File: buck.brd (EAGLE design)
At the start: 100 x 100 mm, 30 parts, among them J1 B06B-HCMKK, J2 POWERPOLE_POWER45A_DRILL, J3 POWERPOLE_POWER45A_DRILL

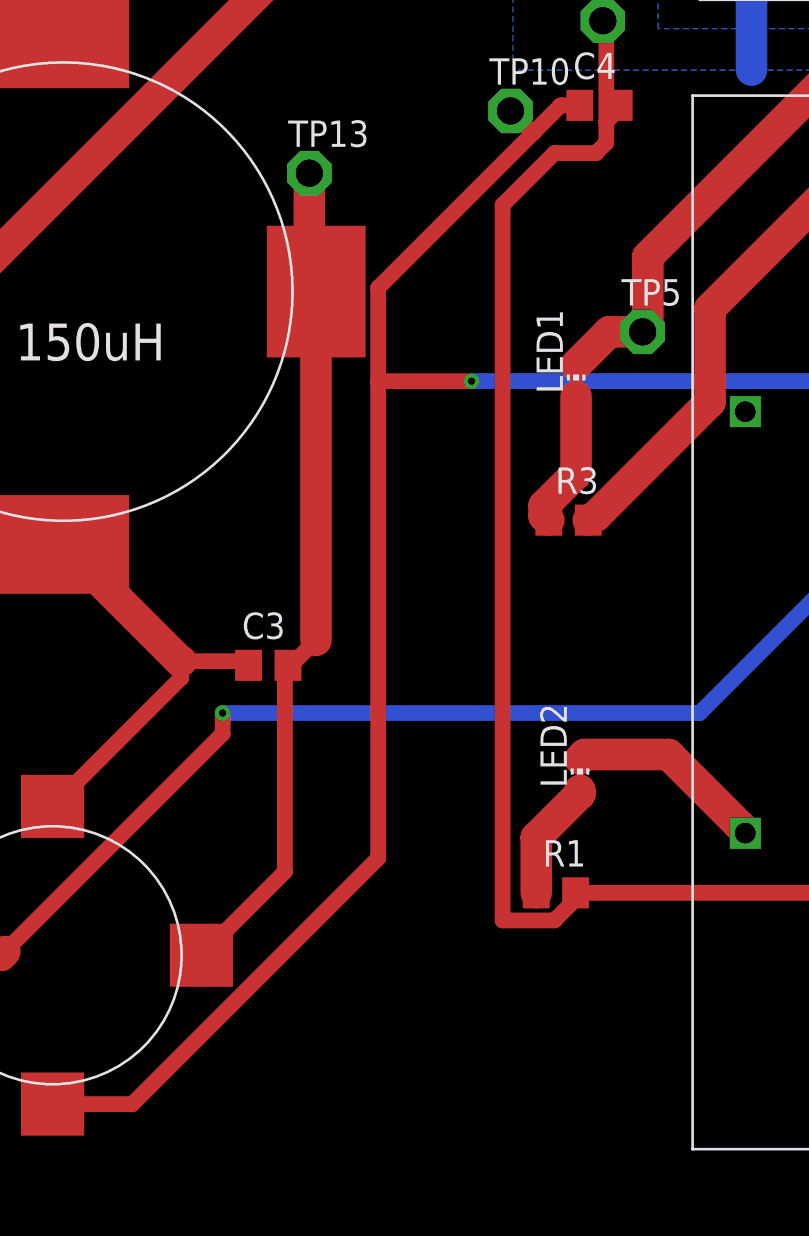
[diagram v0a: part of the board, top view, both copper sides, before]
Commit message: fixed pad clearance
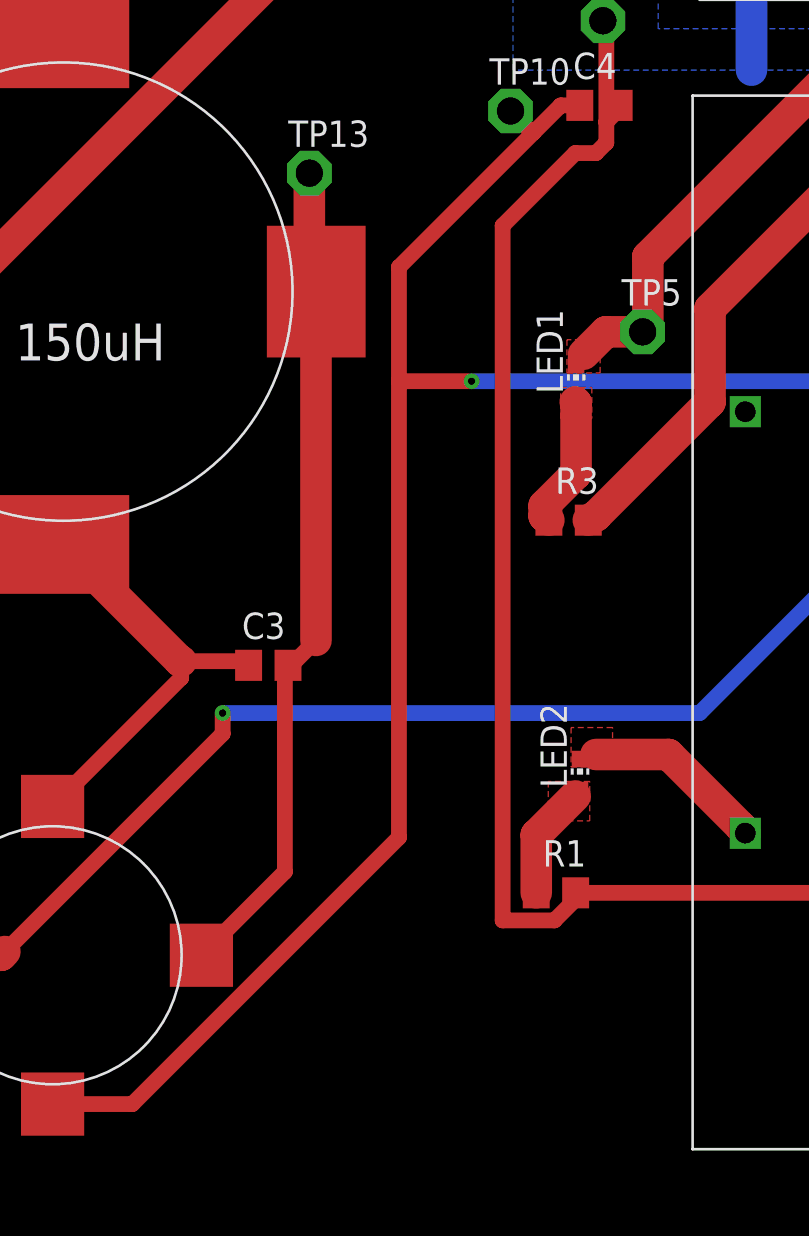
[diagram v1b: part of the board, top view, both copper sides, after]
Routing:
- net N$8: track 122.4 -> 121.4 mm
- net GND: track 109.4 -> 108.6 mm
- net 1.6A_OUT: track 161.3 -> 160.7 mm
- net 6A_GND: track 22.6 -> 22.0 mm
- added copper zone on layer 1, net 6A_GND
- added copper zone on layer 1, net GND
- added copper zone on layer 1, net N$10
- added copper zone on layer 1, net N$24
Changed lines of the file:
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@@
 <?xml version="1.0" encoding="utf-8"?>
 <!DOCTYPE eagle SYSTEM "eagle.dtd">
-<eagle version="9.5.1">
+<eagle version="9.5.0">
 <drawing>
 <settings>
@@
 <wire x1="51.5" y1="36.5" x2="51.5" y2="37" width="1.524" layer="1"/>
 <wire x1="51.5" y1="36.5" x2="51.73" y2="36.3" width="1.524" layer="1"/>
-<wire x1="53.04" y1="38.54" x2="51.5" y2="37" width="1.524" layer="1"/>
-<wire x1="53.04" y1="42.28" x2="53.04" y2="38.54" width="1.524" layer="1"/>
+<wire x1="51.5" y1="37" x2="53.04" y2="38.54" width="1.524" layer="1"/>
+<polygon width="0" layer="1" thermals="no">
+<vertex x="52.3" y="42.7"/>
+<vertex x="53.8" y="42.7"/>
+<vertex x="53.8" y="41.2"/>
+<vertex x="52.3" y="41.2"/>
+</polygon>
+<wire x1="53.04" y1="38.54" x2="53.04" y2="41.96" width="1.524" layer="1"/>
+<wire x1="53.04" y1="41.96" x2="53" y2="42" width="1.524" layer="1"/>
 </signal>
 <signal name="GND" class="1">
@@
 <contactref element="U$3" pad="-VOUT"/>
 <contactref element="C5" pad="2"/>
-<polygon width="0.1524" layer="16">
+<polygon width="0.1524" layer="16" thermals="no">
 <vertex x="50" y="82"/>
 <vertex x="35" y="82"/>
@@
 <via x="32" y="96" extent="1-16" drill="0.35"/>
 <via x="85.5" y="58" extent="1-16" drill="0.35"/>
-<wire x1="53.23" y1="24.78" x2="53.45" y2="25" width="1.524" layer="1"/>
-<wire x1="53.45" y1="25" x2="57.5" y2="25" width="1.524" layer="1"/>
 <wire x1="10.49" y1="58.38" x2="27.188" y2="58.38" width="1.524" layer="1"/>
 <wire x1="27.188" y1="58.38" x2="28.32" y2="59.512" width="1.524" layer="1"/>
+<polygon width="0" layer="1" thermals="no">
+<vertex x="52.8" y="26.3"/>
+<vertex x="52.8" y="24.4"/>
+<vertex x="54.8" y="24.4"/>
+<vertex x="54.8" y="26.3"/>
+</polygon>
+<wire x1="57.5" y1="25" x2="54" y2="25" width="1.524" layer="1"/>
 </signal>
 <signal name="BAT_OUT" class="1">
@@
 <wire x1="54" y1="54" x2="54.5" y2="54.5" width="0.762" layer="1"/>
 <wire x1="54.5" y1="55.5" x2="55" y2="56" width="0.762" layer="1"/>
-<wire x1="52" y1="54" x2="54" y2="54" width="0.762" layer="1"/>
-<wire x1="49.5" y1="51.5" x2="52" y2="54" width="0.762" layer="1"/>
-<wire x1="49.5" y1="17" x2="49.5" y2="51.5" width="0.762" layer="1"/>
+<wire x1="53" y1="54" x2="54" y2="54" width="0.762" layer="1"/>
+<wire x1="49.5" y1="50.5" x2="53" y2="54" width="0.762" layer="1"/>
+<wire x1="49.5" y1="17" x2="49.5" y2="50.5" width="0.762" layer="1"/>
 <wire x1="49.5" y1="17" x2="52" y2="17" width="0.762" layer="1"/>
 <wire x1="55" y1="56" x2="55.12" y2="56.3" width="0.762" layer="1"/>
@@
 <contactref element="U$1" pad="-S"/>
 <contactref element="LED1" pad="C"/>
-<polygon width="0.1524" layer="16">
+<polygon width="0.1524" layer="16" thermals="no">
 <vertex x="104" y="101"/>
 <vertex x="104" y="62"/>
@@
 <via x="66" y="58.5" extent="1-16" drill="0.35"/>
 <wire x1="56.25" y1="45.38" x2="56.5" y2="45.5" width="1.524" layer="1"/>
-<wire x1="56.25" y1="45.38" x2="54.64" y2="45.38" width="1.524" layer="1"/>
-<wire x1="54.64" y1="45.38" x2="53.04" y2="43.78" width="1.524" layer="1"/>
 <wire x1="56.5" y1="49" x2="66" y2="58.5" width="1.524" layer="1"/>
 <wire x1="56.5" y1="45.5" x2="56.5" y2="49" width="1.524" layer="1"/>
+<polygon width="0" layer="1" thermals="no">
+<vertex x="52.6" y="45"/>
+<vertex x="52.6" y="43.4"/>
+<vertex x="54.2" y="43.4"/>
+<vertex x="54.2" y="45"/>
+</polygon>
+<wire x1="54.48" y1="45.38" x2="53.4" y2="44.3" width="1.524" layer="1"/>
+<wire x1="56.25" y1="45.38" x2="54.48" y2="45.38" width="1.524" layer="1"/>
+<wire x1="53.4" y1="44.3" x2="53.04" y2="43.78" width="0" layer="19" extent="1-1"/>
 </signal>
 <signal name="6A_OUT" class="1">
@@
 <wire x1="69" y1="42" x2="83.5" y2="56.5" width="0.762" layer="1"/>
 <wire x1="69" y1="42" x2="68.82" y2="41.53" width="0.762" layer="1"/>
-<wire x1="43.5" y1="47.5" x2="51" y2="55" width="0.762" layer="1"/>
+<wire x1="44.5" y1="48.5" x2="51" y2="55" width="0.762" layer="1"/>
 <wire x1="51" y1="55" x2="52.3" y2="56.3" width="0.762" layer="1"/>
 <wire x1="53.22" y1="56.3" x2="52.3" y2="56.3" width="0.762" layer="1"/>
-<wire x1="43.5" y1="43" x2="43.5" y2="20" width="0.762" layer="1"/>
-<wire x1="43.5" y1="43" x2="43.5" y2="47.5" width="0.762" layer="1"/>
+<wire x1="44.5" y1="43" x2="44.5" y2="21" width="0.762" layer="1"/>
+<wire x1="44.5" y1="43" x2="44.5" y2="48.5" width="0.762" layer="1"/>
 <wire x1="68.5" y1="43" x2="68.5" y2="42" width="0.762" layer="16"/>
 <wire x1="68.5" y1="43" x2="48" y2="43" width="0.762" layer="16"/>
-<wire x1="43.5" y1="43" x2="48" y2="43" width="0.762" layer="1"/>
+<wire x1="44.5" y1="43" x2="48" y2="43" width="0.762" layer="1"/>
 <wire x1="68.5" y1="42" x2="68.82" y2="41.53" width="0.762" layer="16"/>
 <via x="48" y="43" extent="1-16" drill="0.35"/>
 <wire x1="31.6445" y1="8.1445" x2="27.8" y2="8.1445" width="0.762" layer="1"/>
-<wire x1="43.5" y1="20" x2="31.6445" y2="8.1445" width="0.762" layer="1"/>
+<wire x1="44.5" y1="21" x2="31.6445" y2="8.1445" width="0.762" layer="1"/>
 <wire x1="49.88" y1="56.03" x2="50.91" y2="55" width="0.762" layer="1"/>
 <wire x1="50.91" y1="55" x2="51" y2="55" width="0.762" layer="1"/>
@@
 <contactref element="R1" pad="1"/>
 <contactref element="LED2" pad="A"/>
-<wire x1="51.12" y1="20.9936" x2="51.12" y2="18.33" width="1.524" layer="1"/>
-<wire x1="53.23" y1="23.1036" x2="51.12" y2="20.9936" width="1.524" layer="1"/>
-<wire x1="53.23" y1="23.28" x2="53.23" y2="23.1036" width="1.524" layer="1"/>
+<polygon width="0" layer="1" thermals="no">
+<vertex x="51.7" y="23.7"/>
+<vertex x="51.7" y="21.8"/>
+<vertex x="53.7" y="21.8"/>
+<vertex x="53.7" y="23.7"/>
+</polygon>
+<wire x1="51.12" y1="21.12" x2="53" y2="23" width="1.524" layer="1"/>
+<wire x1="51.12" y1="18.33" x2="51.12" y2="21.12" width="1.524" layer="1"/>
 </signal>
 </signals>

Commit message: Add files via upload
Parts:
- removed C1: 10uF, rcl:EU25-10
- removed TP3: TPPAD1-13, testpad:P1-13
- added C2: EEE-FK1J680UP, SamacSys_Parts:CAPAE830X1050N
- added JP1: (no value), jumper:JP1
- C3: value 220uF -> 10 uf
- C6: value 66uF -> UPW2A221MHD; device rcl:C0805 -> SamacSys_Parts:CAPPRD550W60D1050H1750
- moved TP8 98.7 mm to (97.0, 91.4)
- moved C3 71.5 mm to (79.0, 88.0), turned to 90 degrees
- moved C6 68.4 mm to (34.0, 26.0), turned to 270 degrees
- moved TP5 58.7 mm to (97.2, 87.4)
- moved TP6 48.7 mm to (97.2, 83.4)
- moved R3 48.3 mm to (79.7, 76.3), turned to 90 degrees
- moved TP10 47.0 mm to (70.9, 14.0)
- moved C5 45.9 mm to (71.5, 24.3), turned to 270 degrees
- moved TP4 45.9 mm to (97.3, 76.4)
- moved TP1 44.3 mm to (16.1, 55.0)
- moved TP7 42.8 mm to (97.1, 79.4)
- moved LED1 37.5 mm to (79.0, 70.0), turned to 180 degrees
- moved C4 31.6 mm to (72.2, 30.3), turned to 90 degrees
- moved LED2 26.4 mm to (77.2, 13.0), turned to 180 degrees
- moved R1 25.0 mm to (77.1, 18.3), turned to 90 degrees
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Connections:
- removed net N$3: BUCK150UH.2, C3.1, CHOKEME.1, TP12.TP
- new net N$1: BUCK150UH.2, C6.2, CHOKEME.1, TP12.TP
- net 6A_GND: now also C3.2; no longer C1.2
- net 6A_OUT: now also C3.1; no longer C1.1, TP3.TP
- net BAT_OUT: now also C2.1; no longer C6.1
- net GND: now also C2.2; no longer C6.2
- net N$4: now also C6.1; no longer C3.2
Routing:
- net N$1: track 0.00 -> 60.6 mm
- net N$8: track 121.4 -> 66.3 mm, vias 1 -> 0
- net 6A_OUT: track 110.7 -> 58.9 mm
- net 1.6A_OUT: track 160.7 -> 127.5 mm
- net BAT_OUT: track 97.3 -> 66.3 mm
- net N$6: track 68.9 -> 41.0 mm, vias 1 -> 0
- net N$3: track 27.7 -> 0.00 mm
- net RC: track 42.0 -> 23.9 mm
- net N$4: track 40.2 -> 27.0 mm
- net GND: track 108.6 -> 97.1 mm, vias 2 -> 0
- net FUSE: track 41.4 -> 37.4 mm
- net N$10: track 5.45 -> 3.67 mm
- net N$24: track 6.46 -> 4.84 mm
- net 6A_GND: track 22.0 -> 22.8 mm, vias 1 -> 0
- removed copper zone on layer 1, net 6A_GND
- removed copper zone on layer 1, net GND
- removed copper zone on layer 1, net N$10
- removed copper zone on layer 1, net N$24
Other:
- board text added: "RICE SEM 2020 BUCK - REVOLUTION"

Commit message: final touches
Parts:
- F1: value FUSESHK20L -> KEYSTONE_FUSE_3522; device fuse:SHK20L -> AUX Lib:KEYSTONE_FUSE_3522
- moved JP1 72.3 mm to (51.0, 57.0), turned to 90 degrees
- moved TP8 58.1 mm to (45.0, 65.4)
- moved TP5 41.0 mm to (63.2, 64.4)
- moved TP4 38.5 mm to (79.3, 42.4)
- moved TP7 37.1 mm to (64.1, 96.4)
- moved TP12 25.0 mm to (25.5, 9.03)
- moved F1 19.1 mm to (38.9, 91.1), turned to 0 degrees
- moved TP6 18.7 mm to (79.2, 88.4)
- moved TP9 15.0 mm to (33.9, 6.38)
- moved CHOKEME 13.0 mm to (35.8, 19.3), turned to 135 degrees
- moved TP1 11.7 mm to (10.1, 45.0)
- moved C6 10.0 mm to (24.0, 26.0), turned to 225 degrees
- moved C2 9.22 mm to (50.0, 81.0), turned to 270 degrees
- moved LED1 7.81 mm to (80.3, 77.7)
- moved TP13 7.62 mm to (40.2, 39.0)
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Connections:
- net 6A_GND: now also JP1.1
- net BAT_OUT: now also F1.B1, F1.B2; no longer F1.2A
- net FUSE: now also F1.A1, F1.A2; no longer F1.1A
- net GND: now also JP1.2
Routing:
- net RC: track 23.9 -> 65.0 mm
- net 6A_OUT: track 58.9 -> 25.0 mm
- net N$1: track 60.6 -> 34.2 mm
- net GND: track 97.1 -> 72.7 mm, vias 0 -> 14
- net N$6: track 41.0 -> 26.2 mm
- net N$8: track 66.3 -> 53.4 mm
- net FUSE: track 37.4 -> 24.7 mm
- net BAT_OUT: track 66.3 -> 76.0 mm
- net N$24: track 4.84 -> 1.59 mm
- net 6A_GND: track 22.8 -> 20.0 mm, vias 0 -> 1
- net N$4: track 27.0 -> 29.0 mm
- added copper zone on layer 1, net 6A_GND
- added copper zone on layer 1, net 6A_OUT
- added copper zone on layer 1, net BAT_OUT
- added copper zone on layer 1, net FUSE
- added copper zone on layer 1, net GND

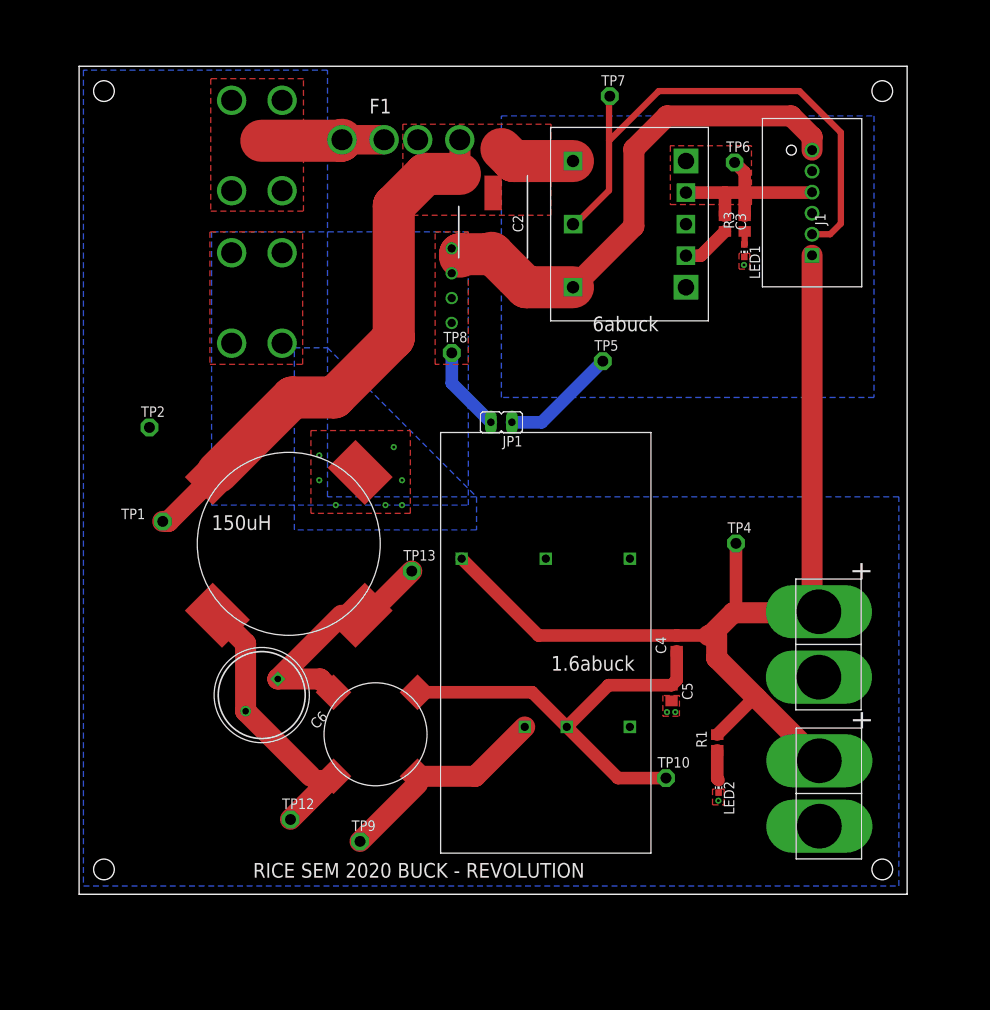
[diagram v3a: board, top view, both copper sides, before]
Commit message: Add silkscreen stuff
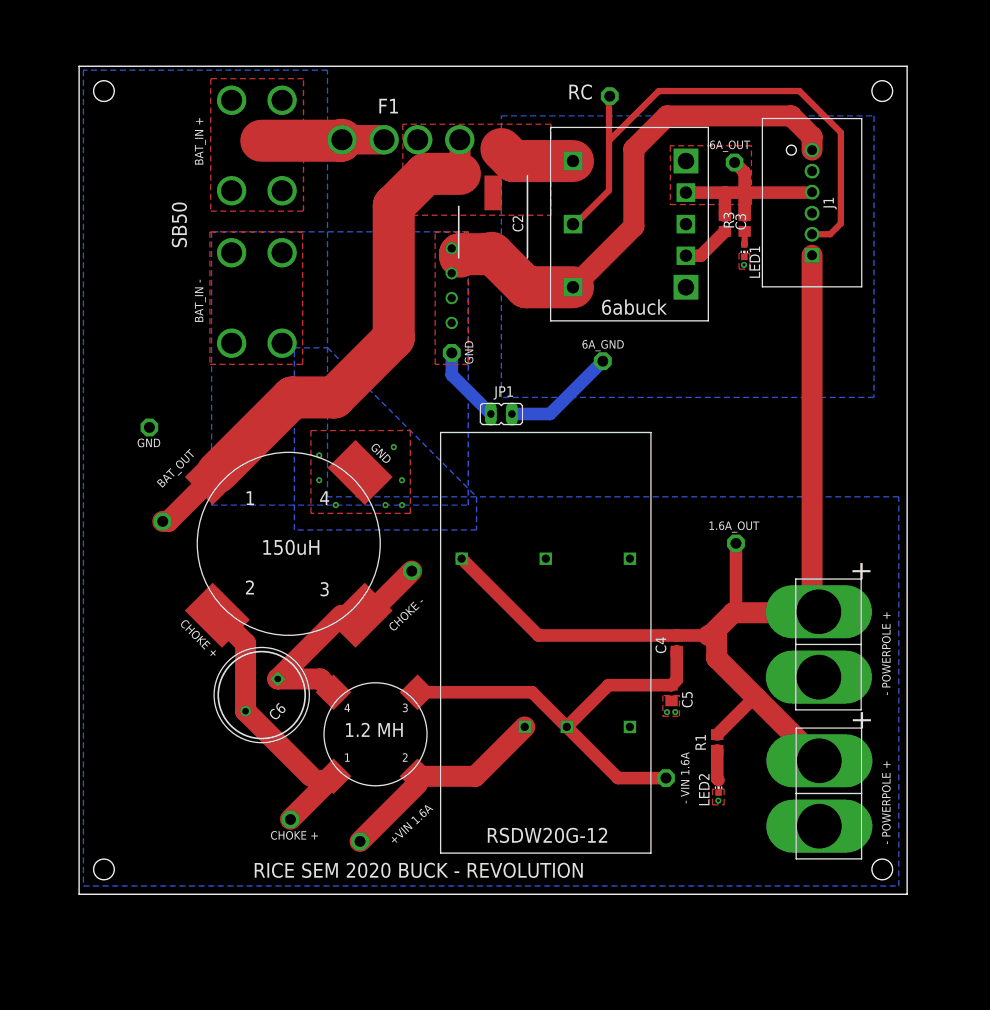
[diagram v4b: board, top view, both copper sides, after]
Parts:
- moved JP1 1.00 mm to (51.0, 58.0)
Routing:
- net GND: track 72.7 -> 71.7 mm
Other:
- board text added: "+VIN 1.6A"
- board text added: "- POWERPOLE +"
- board text added: "- VIN 1.6A"
- board text added: "1"
- board text added: "1.2 MH"
- board text added: "1.6A_OUT"
- board text added: "2"
- board text added: "3"
- board text added: "4"
- board text added: "6A_GND"
- board text added: "6A_OUT"
- board text added: "BAT_IN +"
- board text added: "BAT_IN -"
- board text added: "BAT_OUT"
- board text added: "CHOKE +"
- board text added: "CHOKE -"
- board text added: "GND"
- board text added: "RC"
- board text added: "RSDW20G-12"
- board text added: "SB50"
- board text removed: "1.6abuck"
